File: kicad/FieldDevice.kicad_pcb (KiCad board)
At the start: 2 copper layers, 53.5 x 38.5 mm, 30 parts, among them P201 CONN_01X01, P202 CONN_01X01, SW301 SW_PUSH, U101 DS7505, U301 EA_DOGMxxx-A

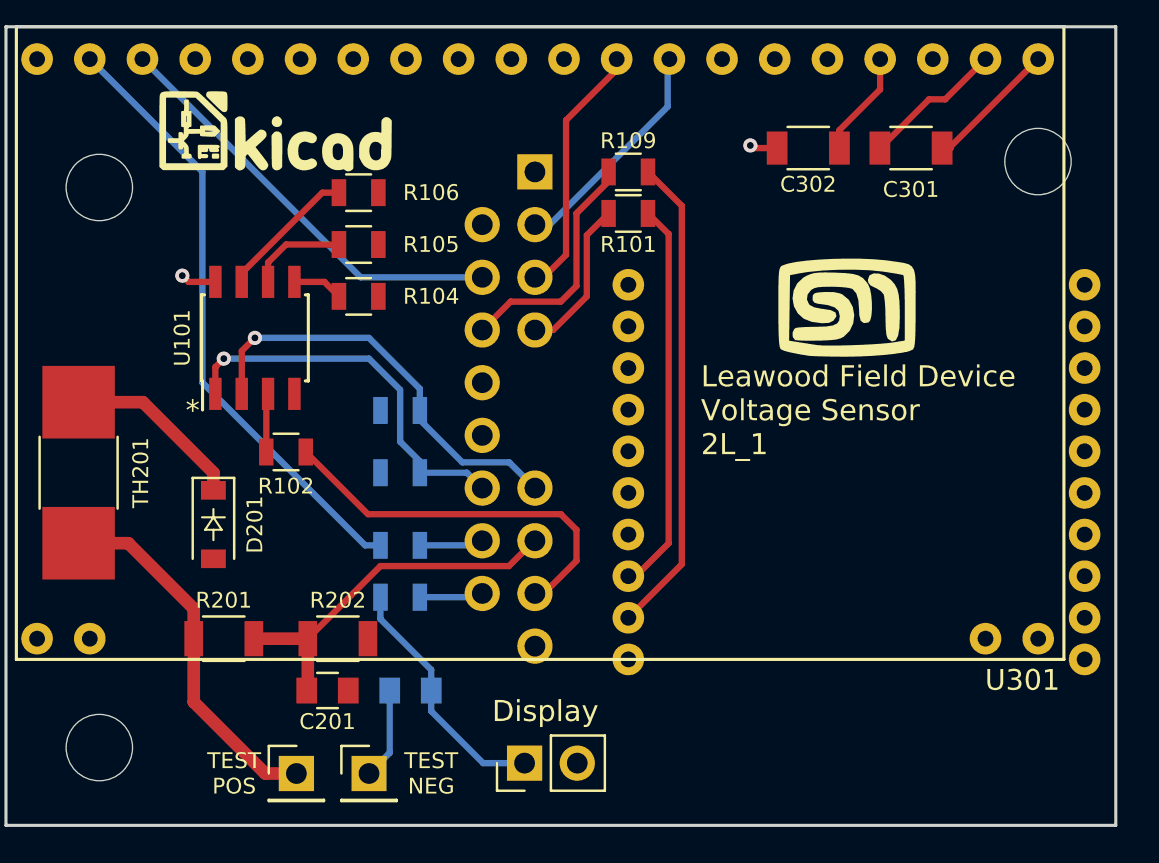
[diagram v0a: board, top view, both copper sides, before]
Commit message: added the missing pullup resistors 2L_2
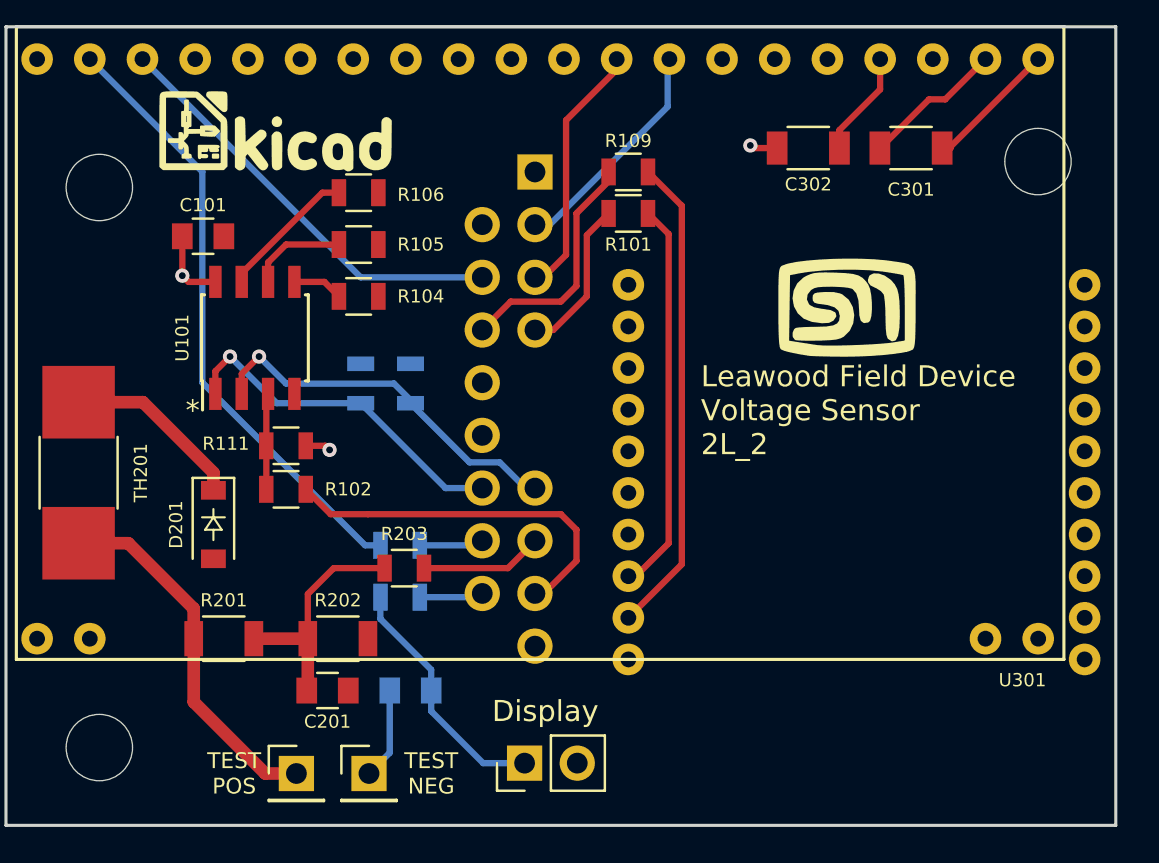
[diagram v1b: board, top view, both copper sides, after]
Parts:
- added C101: 100pF 50V, Capacitors_SMD:C_0805, F.Cu at (117.0, 74.1)
- added R111: 10k, Resistors_SMD:R_0805, F.Cu at (121.0, 84.2)
- added R203: 0Ω, Resistors_SMD:R_0805, F.Cu at (126.7, 90.1)
- moved R110 4.70 mm to (124.6, 81.2), turned to 90 degrees
- moved R102 1.80 mm to (121.0, 86.3)
- moved R103 1.39 mm to (127.0, 81.2), turned to 90 degrees
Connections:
- C201 pad 1: /Analog_Sensors/ANLG_1 -> Net-(C201-Pad1)
- R201 pad 2: /Analog_Sensors/ANLG_1 -> Net-(C201-Pad1)
- R202 pad 1: /Analog_Sensors/ANLG_1 -> Net-(C201-Pad1)
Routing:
- net /Analog_Sensors/ANLG_1: track 18.0 -> 5.94 mm
- net Net-(C201-Pad1): track 0.00 -> 11.5 mm
- net /Display/3V3: track 3.07 -> 6.20 mm, vias 2 -> 3
- net /SCK: track 20.3 -> 18.2 mm
- net /OverTemp: track 2.84 -> 4.94 mm
- net /SDA: track 19.1 -> 17.7 mm
- net Net-(H101-Pad17): track 18.8 -> 18.0 mm
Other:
- board text added: "Leawood Field Device Voltage Sensor 2L_2"
- board text removed: "Leawood Field Device Voltage Sensor 2L_1"

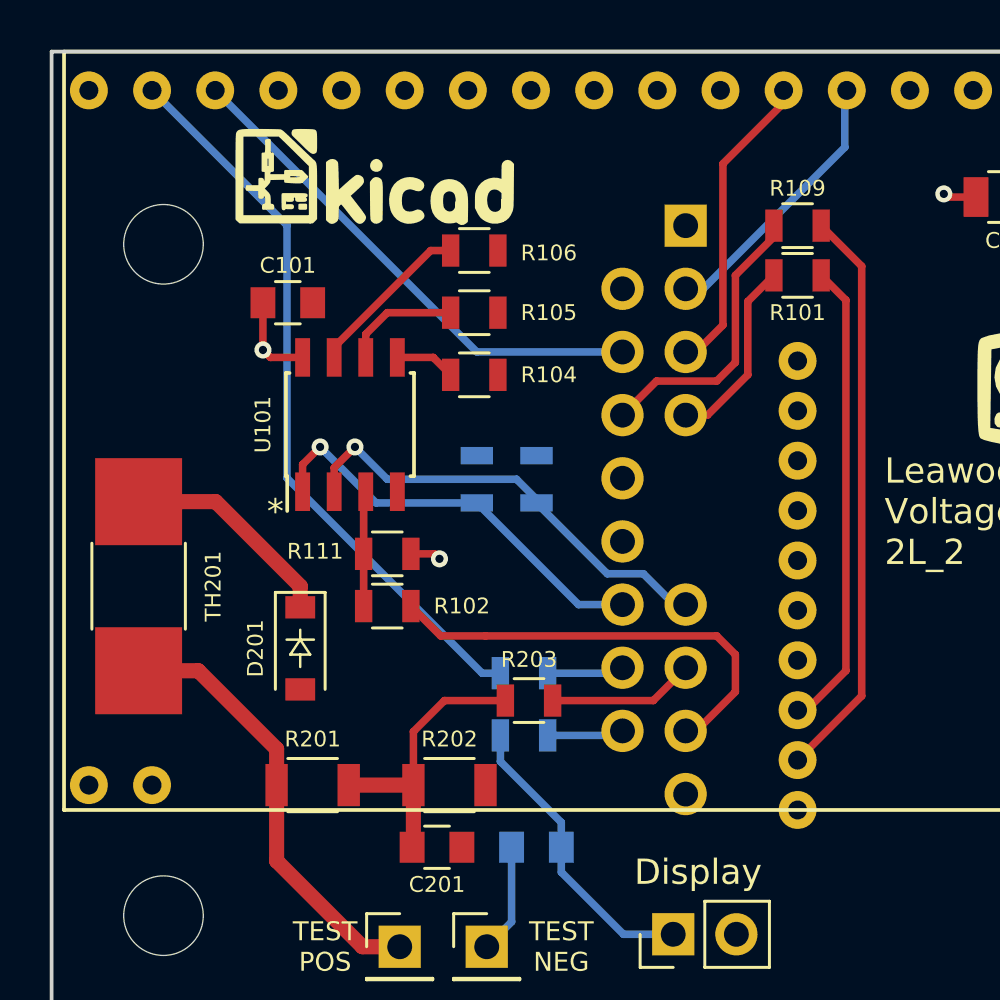
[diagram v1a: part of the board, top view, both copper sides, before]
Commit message: Corrected the usage of the CE_Header to be front-side only
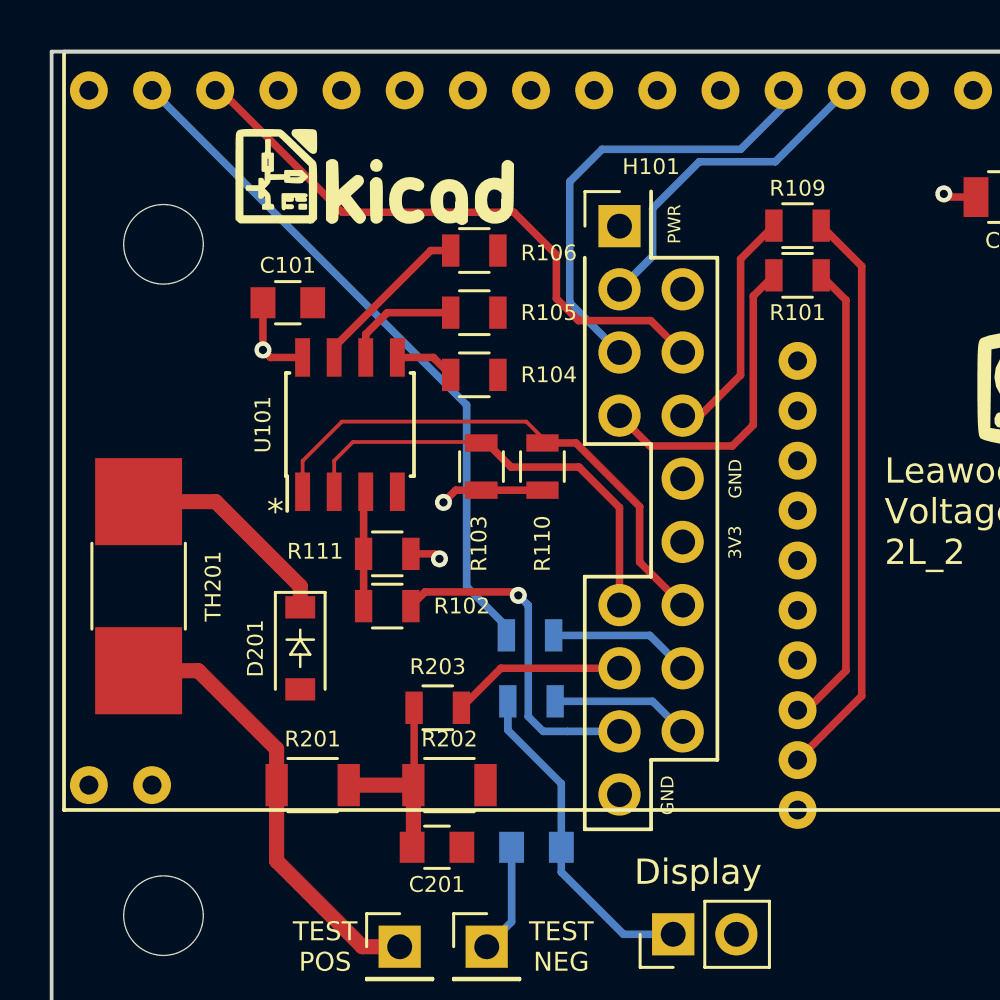
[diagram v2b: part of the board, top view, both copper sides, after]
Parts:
- H101, R103, R110: moved to F.Cu
- moved R203 3.68 mm to (123.0, 90.4)
- moved R110 2.69 mm to (127.2, 80.7), turned to 270 degrees
- moved H101 2.66 mm to (130.3, 71.0), turned to 0 degrees
- moved R103 2.27 mm to (124.8, 80.7), turned to 270 degrees
- moved R107 1.54 mm to (126.7, 87.5)
- moved R108 1.40 mm to (126.8, 90.1)
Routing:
- net /Display/SCK: track 11.9 -> 18.2 mm
- net Net-(H101-Pad7): track 7.61 -> 12.8 mm
- net /Display/3V3: track 6.20 -> 10.4 mm, vias 3 -> 4
- net /SDA: track 17.7 -> 21.7 mm, vias 1 -> 0
- net Net-(H101-Pad17): track 18.0 -> 14.1 mm, vias 0 -> 1
- net /Display/CS: track 20.7 -> 24.3 mm
- net Net-(C201-Pad1): track 11.5 -> 8.24 mm
- net /Display/MOSI: track 10.5 -> 13.8 mm
- net Net-(H101-Pad16): track 3.41 -> 5.74 mm
- net Net-(H101-Pad18): track 3.34 -> 5.66 mm
- net Net-(H101-Pad8): track 11.6 -> 10.0 mm
- net /Display/RS: track 29.7 -> 28.3 mm
- net /Display/Display: track 12.1 -> 13.3 mm
- net /Analog_Sensors/ANLG_1: track 5.94 -> 7.02 mm
- net /SCK: track 18.2 -> 18.5 mm, vias 1 -> 0
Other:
- board text added: "3V3"
- board text added: "GND"
- board text added: "PWR"

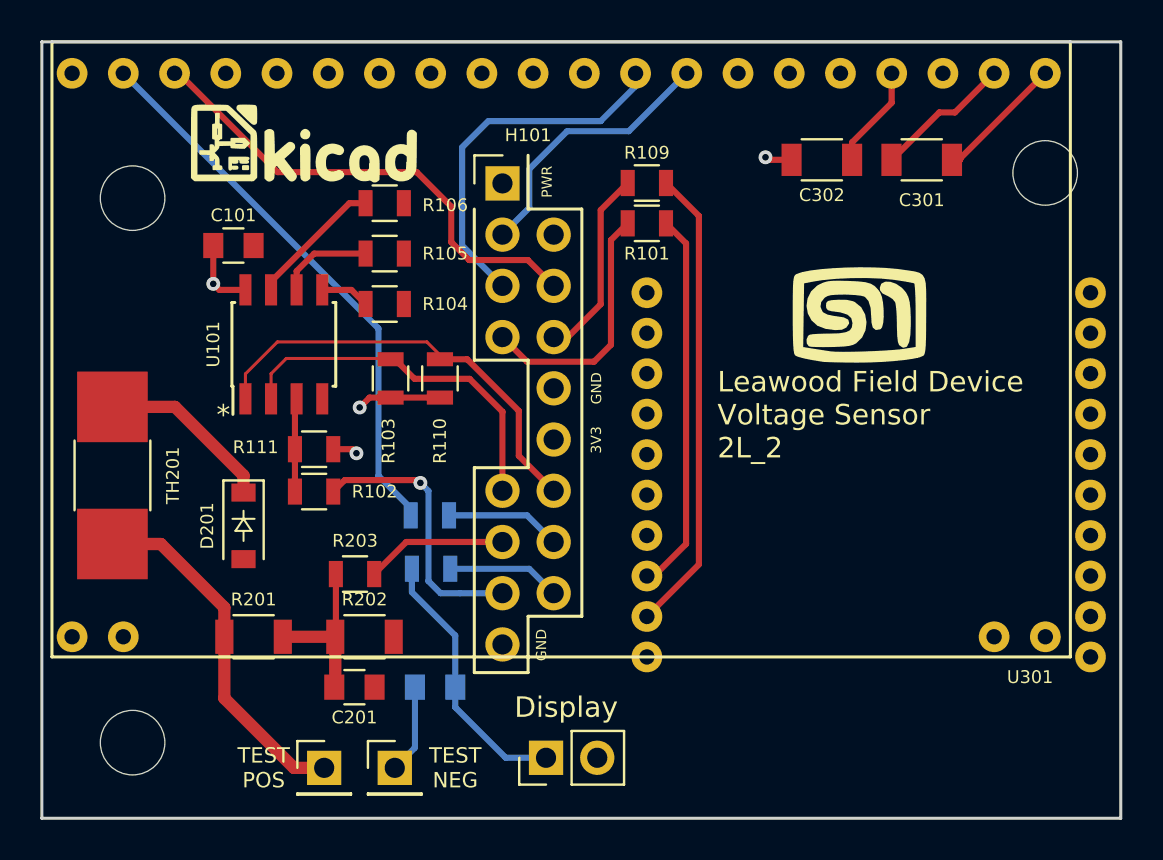
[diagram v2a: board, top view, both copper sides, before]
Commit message: Change over to use the DOGM081 adapter board rather than direct connect - also used the CE_Socket!
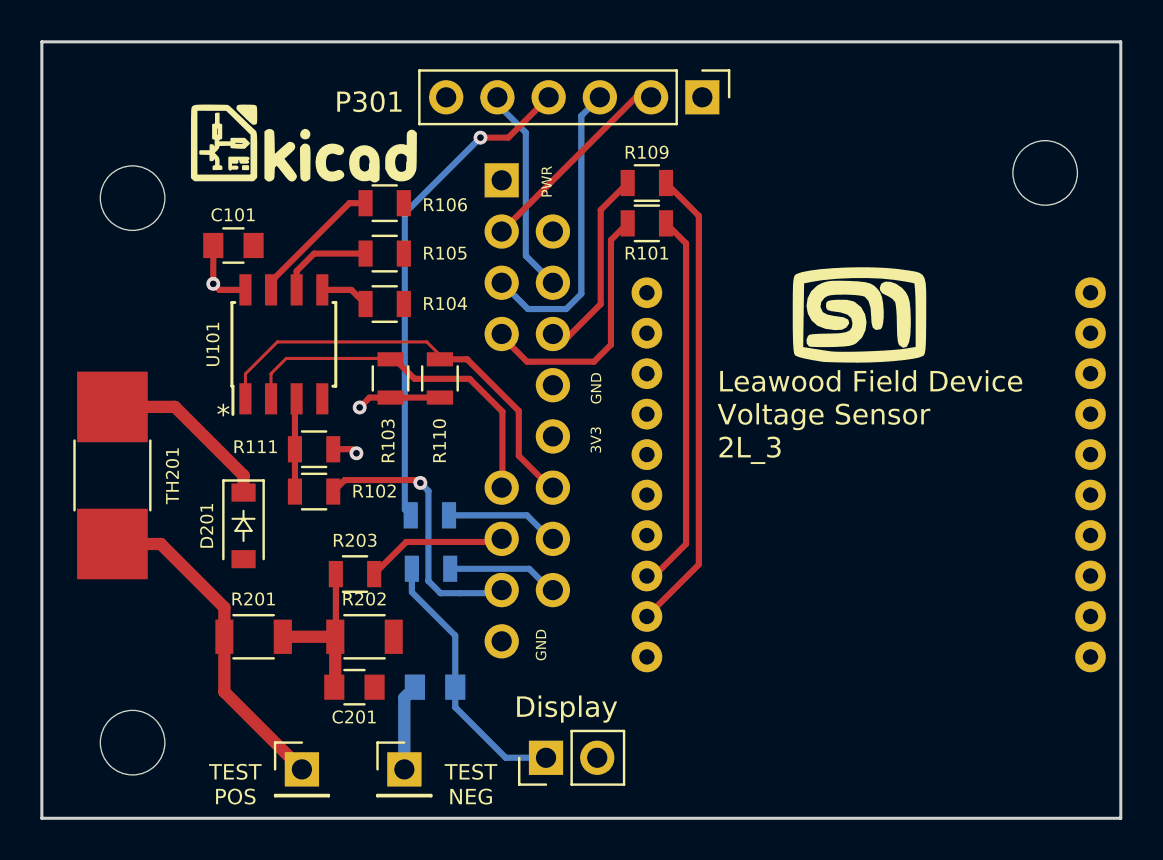
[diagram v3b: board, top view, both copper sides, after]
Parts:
- removed C301: 0.1~~1μF, Capacitors_SMD:C_1206
- removed C302: 0.47~~2.2μF, Capacitors_SMD:C_1206
- removed U301: EA_DOGMxxx-A, FieldDevice_Footprints:EA_DOGM081x-A
- added P301: CONN_01X06, Pin_Headers:Pin_Header_Straight_1x06_Pitch2.54mm, F.Cu at (140.2, 66.8)
- H101: footprint CE_Header:CE_Header -> CE_Header:CE_Socket; moved to B.Cu
- moved H101 2.51 mm to (132.8, 70.9), turned to 180 degrees
- moved P201 1.11 mm to (120.4, 100.1)
- moved P202 0.48 mm to (125.5, 100.1)
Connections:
- H101 pad 1: Net-(H101-Pad1) -> (no net)
- H101 pad 4: Net-(H101-Pad4) -> (no net)
- H102 pad 11: Net-(H102-Pad11) -> (no net)
- H102 pad 12: Net-(H102-Pad12) -> (no net)
- H102 pad 13: Net-(H102-Pad13) -> (no net)
- H102 pad 14: Net-(H102-Pad14) -> (no net)
- H102 pad 15: Net-(H102-Pad15) -> (no net)
- H102 pad 16: Net-(H102-Pad16) -> (no net)
- H102 pad 17: Net-(H102-Pad17) -> (no net)
- H102 pad 18: Net-(H102-Pad18) -> (no net)
- H102 pad 19: Net-(H102-Pad19) -> (no net)
- H102 pad 20: Net-(H102-Pad20) -> (no net)
- H102 pad 4: Net-(H102-Pad4) -> (no net)
- H102 pad 5: Net-(H102-Pad5) -> (no net)
- H102 pad 6: Net-(H102-Pad6) -> (no net)
- H102 pad 7: Net-(H102-Pad7) -> (no net)
- H102 pad 8: Net-(H102-Pad8) -> (no net)
- H102 pad 9: Net-(H102-Pad9) -> (no net)
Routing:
- net /Display/CS: track 24.3 -> 10.3 mm
- net Net-(C301-Pad1): track 6.87 -> 0.00 mm
- net Net-(C301-Pad2): track 6.45 -> 0.00 mm
- net Net-(C302-Pad1): track 5.10 -> 0.00 mm
- net /Display/MOSI: track 13.8 -> 10.2 mm
- net /Display/SCK: track 18.2 -> 14.9 mm
- net /Display/RS: track 28.3 -> 25.1 mm, vias 0 -> 1
- net /Display/3V3: track 10.4 -> 9.04 mm, vias 4 -> 3
- net /Analog_Sensors/TEST_POS_1: track 17.8 -> 16.6 mm
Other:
- board text added: "Leawood Field Device Voltage Sensor 2L_3"
- board text removed: "Leawood Field Device Voltage Sensor 2L_2"

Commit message: Enhanced display port connector and layout - Submit to OSH Park
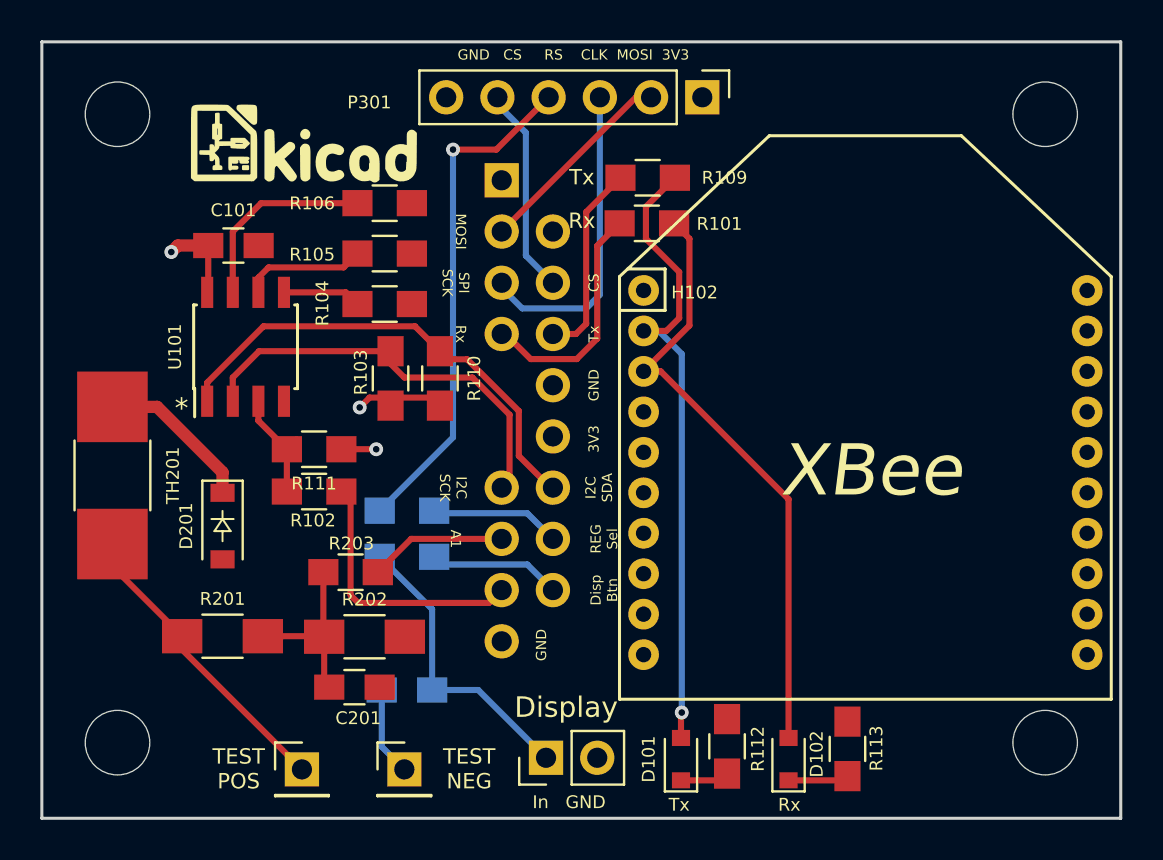
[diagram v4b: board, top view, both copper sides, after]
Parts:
- added D101: LED, Diodes_SMD:D_0805, F.Cu at (139.2, 99.6)
- added D102: LED, Diodes_SMD:D_0805, F.Cu at (144.5, 99.6)
- added R112: 680Ω, Resistors_SMD:R_0805_HandSoldering, F.Cu at (141.5, 98.9)
- added R113: 680Ω, Resistors_SMD:R_0805_HandSoldering, F.Cu at (147.4, 99.1)
- added REF**: MountingHole_3.2mm_M3, Mounting_Holes:MountingHole_3.2mm_M3, F.Cu at (157.2, 98.8)
- C101, C201, C303: footprint Capacitors_SMD:C_0805 -> Capacitors_SMD:C_0805_HandSoldering
- G***: moved to B.Cu
- H101: value CE_Header -> CE_Socket
- H102: moved to F.Cu
- P201: value CONN_01X01 -> Positive
- P202: value CONN_01X01 -> Negative
- R101, R102, R103, R104, R105, R106, R107, R108, R109, R110, R111, R203: footprint Resistors_SMD:R_0805 -> Resistors_SMD:R_0805_HandSoldering
- R201: value 100kΩ 0.1% -> 1MΩ 125mW 0.1%; footprint Resistors_SMD:R_1206 -> Resistors_SMD:R_1206_HandSoldering
- R202: value 39kΩ 0.1% -> 30kΩ 125mW 0.1%; footprint Resistors_SMD:R_1206 -> Resistors_SMD:R_1206_HandSoldering
- moved H102 18.2 mm to (148.3, 76.3)
- moved REF** 4.23 mm to (111.3, 67.6)
- moved REF** 2.91 mm to (157.2, 67.6)
- moved U101 1.90 mm to (117.6, 79.1)
- moved G*** 1.81 mm to (148.9, 75.9), turned to 180 degrees
- moved R201 1.54 mm to (116.5, 93.5)
- moved C303 1.40 mm to (125.6, 96.1)
- moved R108 1.34 mm to (125.6, 89.5)
- moved R107 1.16 mm to (125.6, 87.2)
- moved D201 1.04 mm to (116.5, 88.0)
- moved REF** 0.75 mm to (111.3, 98.8)
- moved R109 0.26 mm to (137.5, 70.7)
- moved R203 0.24 mm to (122.8, 90.3)
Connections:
- net /Display/SCK renamed /Display/SPI_SCK
- net /SCK renamed /I2C_SCK
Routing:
- net /RX: track 18.9 -> 30.3 mm
- net /TX: track 23.2 -> 32.7 mm, vias 0 -> 1
- net Net-(R106-Pad1): track 6.71 -> 10.6 mm
- net /I2C_SCK: track 18.5 -> 21.7 mm
- net Net-(D102-Pad1): track 0.00 -> 3.01 mm
- net Net-(D101-Pad1): track 0.00 -> 2.42 mm
- net /SDA: track 21.7 -> 24.0 mm
- net /Display/3V3: track 9.04 -> 11.2 mm
- net Net-(R104-Pad1): track 2.43 -> 3.88 mm
- net Net-(R105-Pad1): track 4.71 -> 6.14 mm
- net /Display/Display: track 13.3 -> 14.7 mm
- net /Analog_Sensors/TEST_POS_1: track 16.6 -> 15.2 mm
- net Net-(D201-Pad1): track 9.86 -> 8.92 mm
- net Net-(H101-Pad18): track 5.66 -> 6.57 mm
- net /OverTemp: track 4.94 -> 5.75 mm
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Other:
- board text added: "A1"
- board text added: "CS"
- board text added: "Disp Btn"
- board text added: "GND CS RS CLK MOSI 3V3"
- board text added: "I2C SCK"
- board text added: "I2C SDA"
- board text added: "In GND"
- board text added: "MOSI"
- board text added: "REG Sel"
- board text added: "Rx"
- board text added: "SPI SCK"
- board text added: "Tx"
